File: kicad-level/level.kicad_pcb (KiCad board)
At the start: 2 copper layers, 62.9 x 27.4 mm, 6 parts, among them J1 Conn_01x01_Pin, J2 Conn_01x08_Pin, J3 Conn_01x01_Pin, U1 ULN2803A_C845537

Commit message: Revert "erreur pcb, com a la masse"
This reverts commit de789b6cb290ad22ceee4c73f03ad83cfbf3b982.
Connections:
- U1 pad 10: unconnected-(U1-COM-Pad10) -> GND
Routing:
- net GND: track 0.00 -> 16.3 mm
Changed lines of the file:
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@@
 	(net 25 "Net-(J2-Pin_8)")
 	(net 26 "GND")
-	(net 27 "unconnected-(U1-COM-Pad10)")
 	(footprint "Connector_PinHeader_2.54mm:PinHeader_1x08_P2.54mm_Vertical"
 		(layer "F.Cu")
@@
 			(layers "F.Cu" "F.Mask" "F.Paste")
 			(roundrect_rratio 0.25)
-			(net 27 "unconnected-(U1-COM-Pad10)")
+			(net 26 "GND")
 			(pinfunction "COM")
 			(pintype "passive")
@@
 		(net 25)
 	)
+	(segment
+		(start 173.355 92.837)
+		(end 173.355 92.329)
+		(width 0.2)
+		(layer "F.Cu")
+		(net 26)
+	)
+	(segment
+		(start 182.905 92.837)
+		(end 173.355 92.837)
+		(width 0.5)
+		(layer "F.Cu")
+		(net 26)
+	)
+	(segment
+		(start 173.355 92.329)
+		(end 168.91 87.884)
+		(width 0.2)
+		(layer "F.Cu")
+		(net 26)
+	)
 	(zone

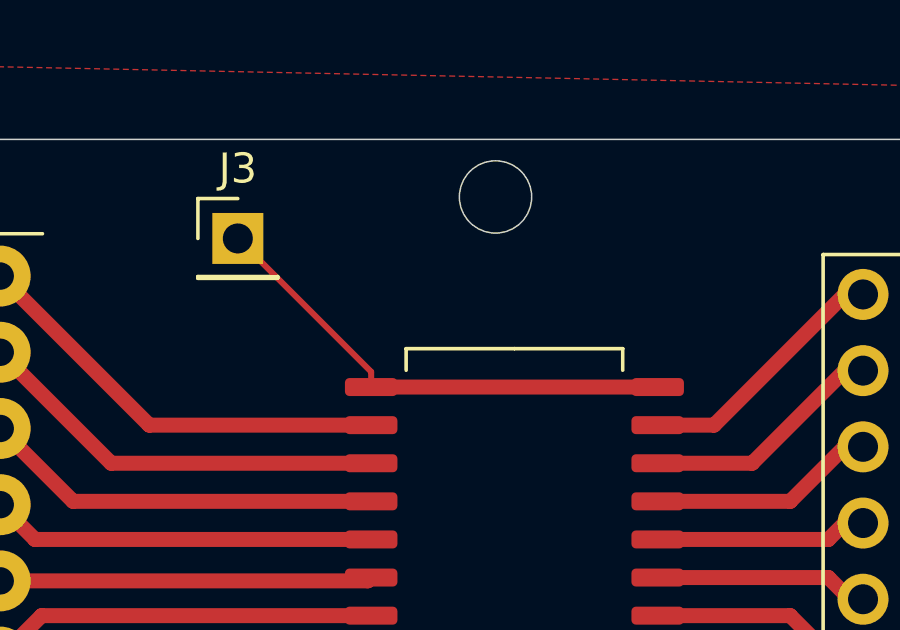
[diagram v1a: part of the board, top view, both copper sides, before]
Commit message: erreur pcb, com a la masse
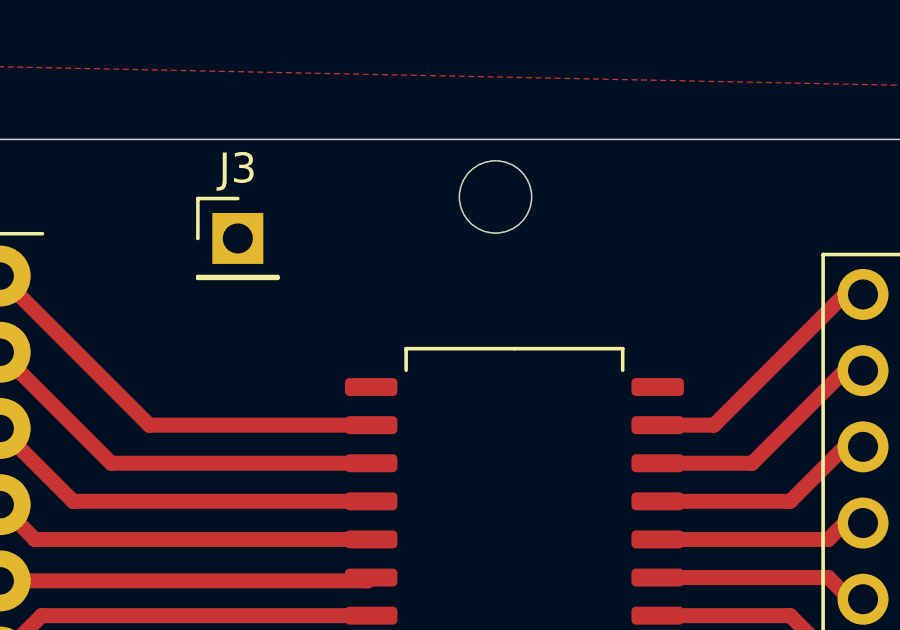
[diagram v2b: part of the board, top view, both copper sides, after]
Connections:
- U1 pad 10: GND -> unconnected-(U1-COM-Pad10)
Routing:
- net GND: track 16.3 -> 0.00 mm
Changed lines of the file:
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@@
 	(net 25 "Net-(J2-Pin_8)")
 	(net 26 "GND")
+	(net 27 "unconnected-(U1-COM-Pad10)")
 	(footprint "Connector_PinHeader_2.54mm:PinHeader_1x08_P2.54mm_Vertical"
 		(layer "F.Cu")
@@
 			(layers "F.Cu" "F.Mask" "F.Paste")
 			(roundrect_rratio 0.25)
-			(net 26 "GND")
+			(net 27 "unconnected-(U1-COM-Pad10)")
 			(pinfunction "COM")
 			(pintype "passive")
@@
 		(net 25)
 	)
-	(segment
-		(start 173.355 92.837)
-		(end 173.355 92.329)
-		(width 0.2)
-		(layer "F.Cu")
-		(net 26)
-	)
-	(segment
-		(start 182.905 92.837)
-		(end 173.355 92.837)
-		(width 0.5)
-		(layer "F.Cu")
-		(net 26)
-	)
-	(segment
-		(start 173.355 92.329)
-		(end 168.91 87.884)
-		(width 0.2)
-		(layer "F.Cu")
-		(net 26)
-	)
 	(zone
